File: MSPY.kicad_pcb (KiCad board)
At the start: 2 copper layers, 15.7 x 43.4 mm, 9 parts, among them J1 Conn_01x12, J2 Conn_01x12, J3 Conn_01x06, SW1 SW_Push, U1 MSP430FR2433RGE

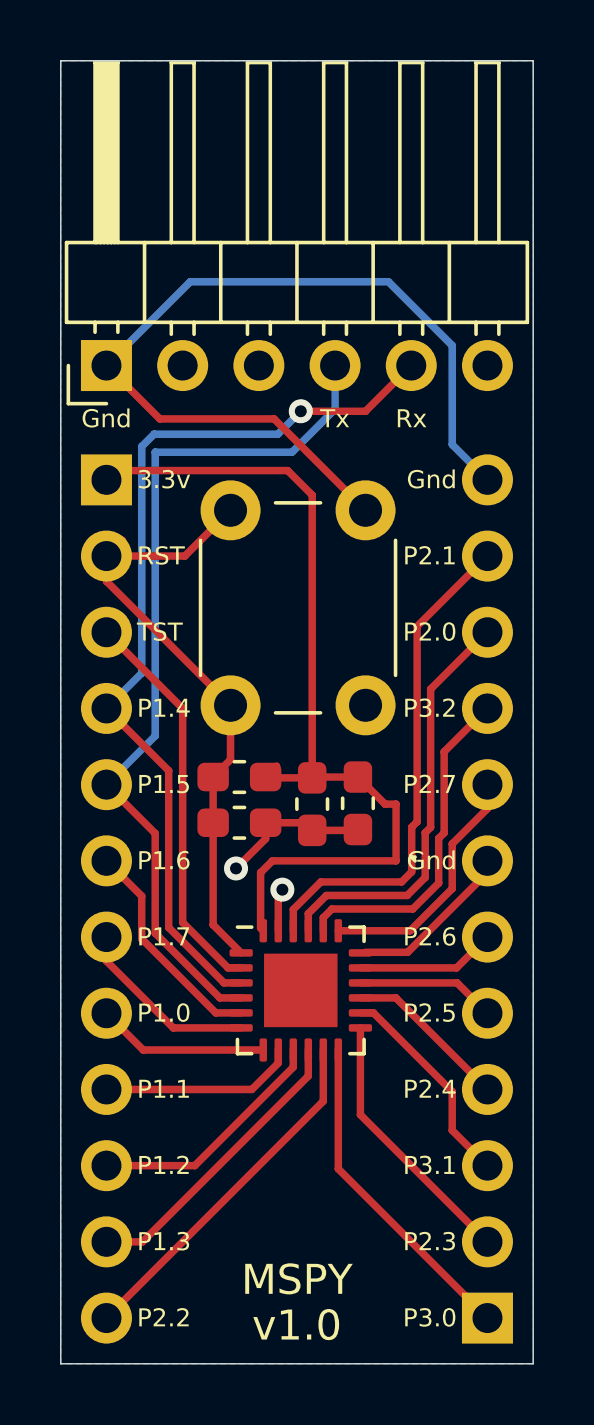
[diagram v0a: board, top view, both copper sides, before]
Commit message: Update to kicad 6 and add UART selector
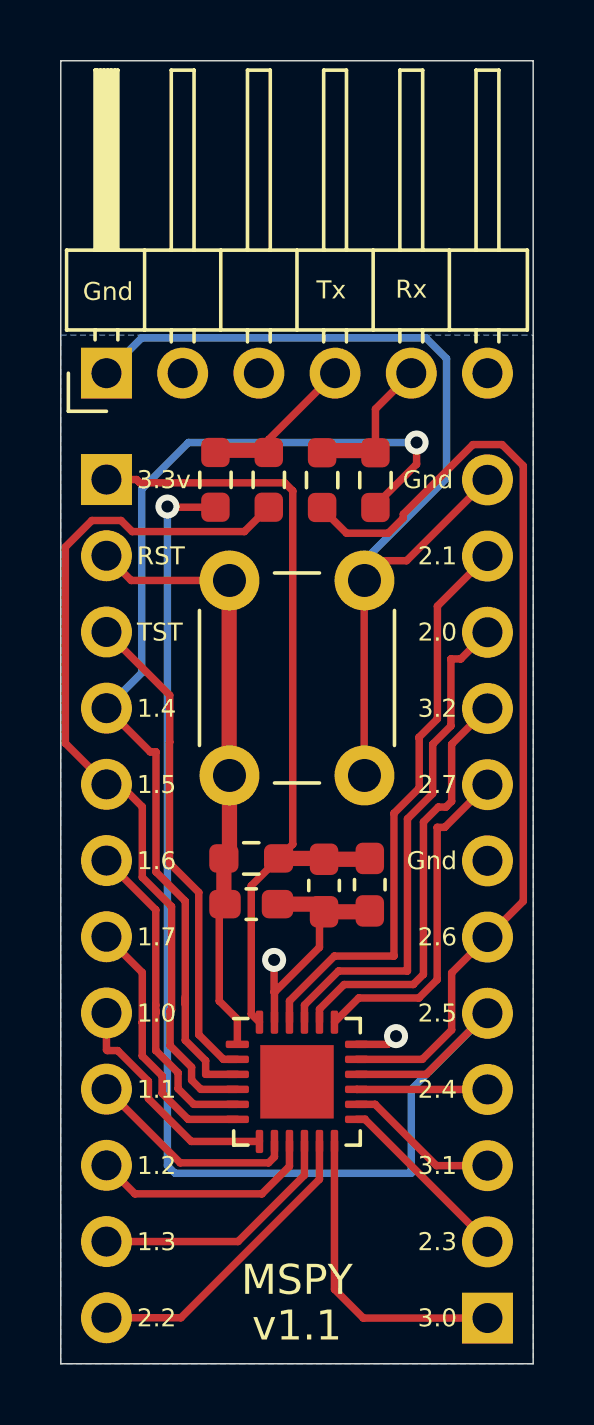
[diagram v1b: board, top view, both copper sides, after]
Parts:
- added R2: 0, Resistor_SMD:R_0603_1608Metric_Pad0.98x0.95mm_HandSolder, F.Cu at (151.0, 68.6)
- added R3: 0, Resistor_SMD:R_0603_1608Metric_Pad0.98x0.95mm_HandSolder, F.Cu at (156.3, 68.6)
- added R4: 0, Resistor_SMD:R_0603_1608Metric_Pad0.98x0.95mm_HandSolder, F.Cu at (154.5, 68.6)
- added R5: 47k, Resistor_SMD:R_0603_1608Metric_Pad0.98x0.95mm_HandSolder, F.Cu at (152.1, 81.2)
- J1: value Conn_01x12 -> Conn_01x06; footprint Connector_PinHeader_2.54mm:PinHeader_1x12_P2.54mm_Vertical -> Connector_PinHeader_2.54mm:PinHeader_1x06_P2.54mm_Horizontal; moved to F.Cu
- J3: value Conn_01x06 -> Conn_01x12; footprint Connector_PinHeader_2.54mm:PinHeader_1x06_P2.54mm_Horizontal -> Connector_PinHeader_2.54mm:PinHeader_1x12_P2.54mm_Vertical; moved to B.Cu
- R1: value 47k -> 0; footprint Resistor_SMD:R_0603_1608Metric_Pad1.05x0.95mm_HandSolder -> Resistor_SMD:R_0603_1608Metric_Pad0.98x0.95mm_HandSolder
- moved J3 34.2 mm to (160.0, 96.5), turned to 0 degrees
- moved J2 30.7 mm to (147.3, 68.6), turned to 180 degrees
- moved R1 9.95 mm to (152.7, 68.6), turned to 90 degrees
- moved J1 3.56 mm to (147.3, 65.0), turned to 90 degrees
- moved U1 3.05 mm to (153.7, 88.6)
- moved C2 2.74 mm to (154.6, 82.1)
- moved C1 2.74 mm to (156.1, 82.1)
- moved C3 2.74 mm to (152.1, 82.7)
- moved SW1 2.34 mm to (151.4, 78.4)
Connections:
- J1 pad 1: VCC -> VSS
- J1 pad 2: P1 -> unconnected-(J1-Pad2)
- J1 pad 3: P2 -> unconnected-(J1-Pad3)
- J1 pad 4: P3 -> RX
- J1 pad 5: P4 -> TX
- J1 pad 6: P5 -> unconnected-(J1-Pad6)
- J2 pad 1: P12 -> VCC
- J2 pad 10: P21 -> P9
- J2 pad 11: P22 -> P10
- J2 pad 12: VSS -> P11
- J2 pad 2: P13 -> P1
- J2 pad 3: P14 -> P2
- J2 pad 4: P15 -> P3
- J2 pad 5: P16 -> P4
- J2 pad 6: P17 -> P5
- J2 pad 7: VSS -> P6
- J2 pad 8: P19 -> P7
- J2 pad 9: P20 -> P8
- J3 pad 1: VSS -> P12
- J3 pad 2: Net-(J3-Pad2) -> P13
- J3 pad 3: Net-(J3-Pad3) -> P14
- J3 pad 4: P4 -> P15
- J3 pad 5: P3 -> P16
- J3 pad 6: Net-(J3-Pad6) -> P17
- R1 pad 1: VCC -> P4
- R1 pad 2: P1 -> RX
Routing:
- net P16: track 4.65 -> 43.4 mm, vias 0 -> 1
- net P17: track 4.66 -> 32.0 mm
- net RX: track 0.00 -> 5.34 mm
- net TX: track 0.00 -> 4.92 mm
- net P3: track 30.7 -> 35.3 mm
- net P5: track 7.42 -> 10.9 mm
- net P1: track 24.1 -> 20.8 mm
- net P21: track 14.0 -> 17.1 mm
- net P2: track 13.3 -> 16.3 mm
- net P20: track 11.3 -> 14.3 mm
- net P19: track 8.33 -> 11.4 mm
- net VCC: track 30.7 -> 27.8 mm
- net P13: track 8.89 -> 6.05 mm
- net P22: track 16.7 -> 19.4 mm
- net P6: track 6.21 -> 8.85 mm
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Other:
- net class Default removed
- rule pad_to_mask_clearance: 0.05 -> 0
- board text added: "1.0"
- board text added: "1.1"
- board text added: "1.2"
- board text added: "1.3"
- board text added: "1.4"
- board text added: "1.5"
- board text added: "1.6"
- board text added: "1.7"
- board text added: "2.0"
- board text added: "2.1"
- board text added: "2.2"
- board text added: "2.3"
- board text added: "2.4"
- board text added: "2.5"
- board text added: "2.6"
- board text added: "2.7"
- board text added: "3.0"
- board text added: "3.1"
- board text added: "3.2"
- board text added: "v1.1"
- board text removed: "P1.0"
- board text removed: "P1.1"
- board text removed: "P1.2"
- board text removed: "P1.3"
- board text removed: "P1.4"
- board text removed: "P1.5"
- board text removed: "P1.6"
- board text removed: "P1.7"
- board text removed: "P2.0"
- board text removed: "P2.1"
- board text removed: "P2.2"
- board text removed: "P2.3"
- board text removed: "P2.4"
- board text removed: "P2.5"
- board text removed: "P2.6"
- board text removed: "P2.7"
- board text removed: "P3.0"
- board text removed: "P3.1"
- board text removed: "P3.2"
- board text removed: "v1.0"
